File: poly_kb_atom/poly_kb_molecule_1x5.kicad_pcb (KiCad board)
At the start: 2 copper layers, 19.1 x 95.2 mm, 174 parts, among them J1 Conn_01x16, J2 North, J3 WestFront, J4 EastFront, J5 WestBack, J6 EastBack, J7 South, J8 North2, J9 South2, SW1 SW_Push

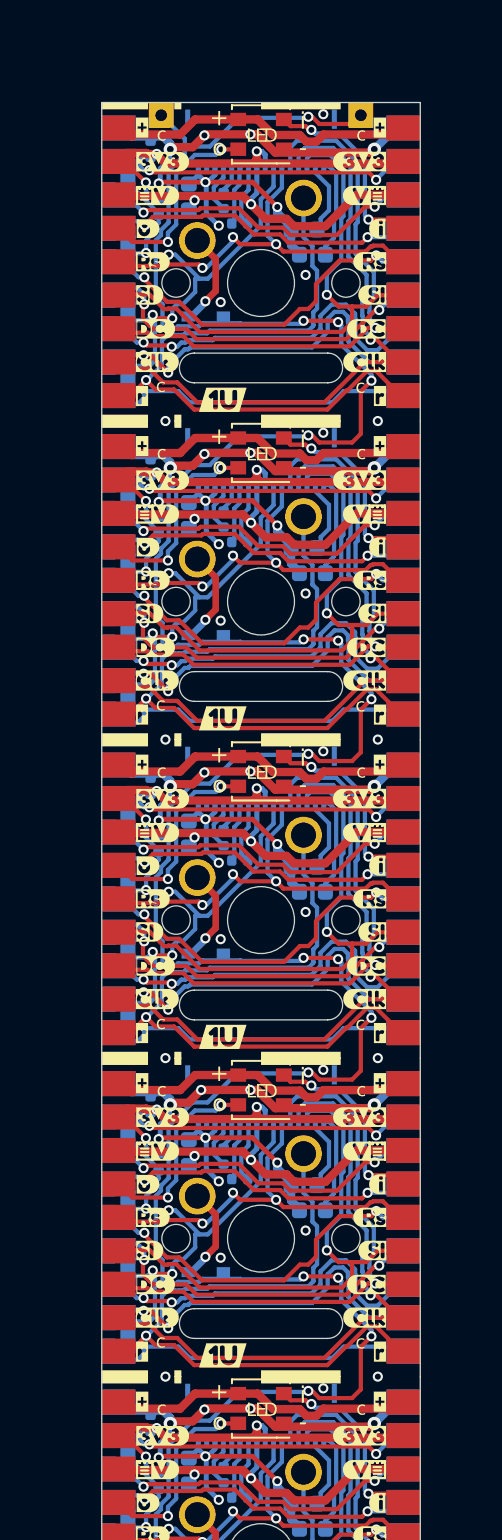
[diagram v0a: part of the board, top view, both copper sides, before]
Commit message: Added optional C7 and fix LED silkscreens
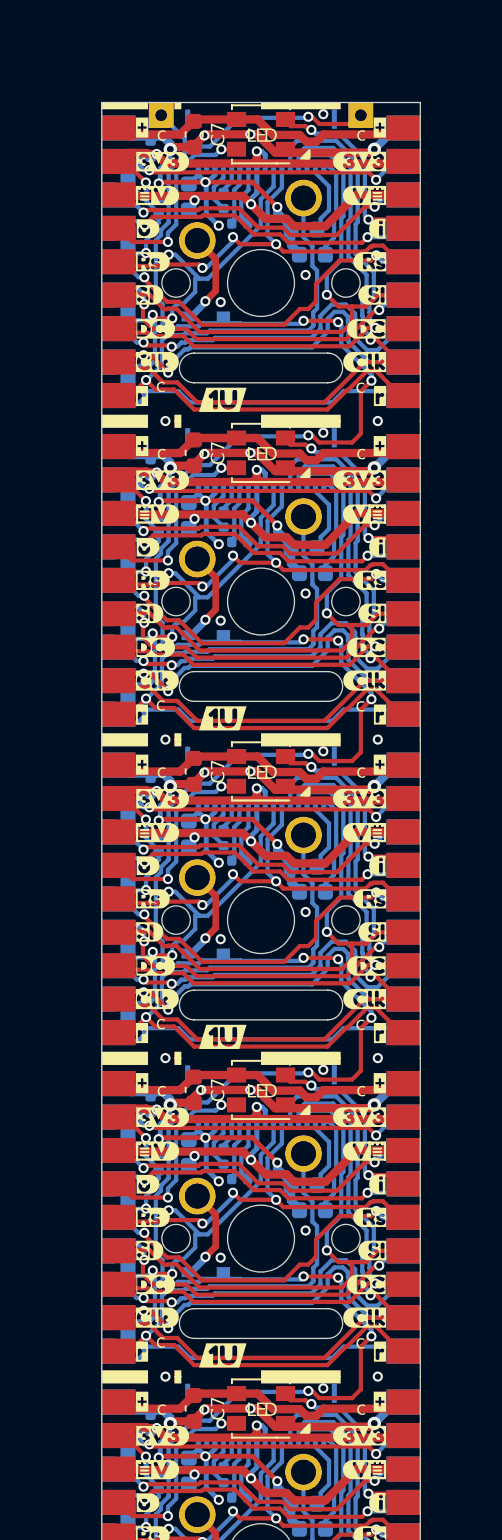
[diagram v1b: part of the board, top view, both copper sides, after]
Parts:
- added C7: 100nF, Capacitor_SMD:C_0603_1608Metric, F.Cu at (59.6, 18.0)
- added C7: 100nF, Capacitor_SMD:C_0603_1608Metric, F.Cu at (59.6, 37.0)
- added C7: 100nF, Capacitor_SMD:C_0603_1608Metric, F.Cu at (59.6, 75.1)
- added C7: 100nF, Capacitor_SMD:C_0603_1608Metric, F.Cu at (59.6, 94.2)
- added C7: 100nF, Capacitor_SMD:C_0603_1608Metric, F.Cu at (59.6, 56.1)
- LED1 (x5): value LED -> WS2812B-Mini
